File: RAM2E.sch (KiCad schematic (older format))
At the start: 54 parts, among them J1 AppleIIeAux, U1 EPM240T100, U2 W9864G6KH-6, U3 74AHC245, U4 74AHC245, U5 74AHC245, U6 74AHCT245, U7 74AHCT245, U8 TPS73701, U9 TPS73701

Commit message: Sent to JLCPCB
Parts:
- removed C? (x2): 2u2, stdpads:C_0603, symbol Device:C_Small
- added C29: 10u, stdpads:C_0805, symbol Device:C_Small
- added H5: (no value), stdpads:PasteHole_1.1mm_PTH, symbol Mechanical:MountingHole_Pad
- added J2: JTAG, Connector:Tag-Connect_TC2050-IDC-FP_2x05_P1.27mm_Vertical, symbol Connector_Generic:Conn_02x05_Odd_Even
- added R5, R7: DNP, stdpads:R_0805, symbol Device:R_Small
- added R6: 0, stdpads:R_0805, symbol Device:R_Small
- added RN1, RN2, RN3: 4x100, stdpads:Yageo_YC124, symbol Device:R_Pack04
- R1: value 1k2 -> 5k76
- R2, R3: value 1k2 -> 3k3
- R4: value 1k2 -> 6k8
- R8: renamed from R5; footprint (none) -> stdpads:R_0805
- U1: value EPM240T100 -> 5M240ZT100; footprint Package_QFP:LQFP-100_14x14mm_P0.5mm -> stdpads:TQFP-100_14x14mm_P0.5mm; symbol CPLD_Altera:EPM240T100 -> GW_PLD:5M240ZT100
- U2: footprint stdpads:Winbond_TSOPII-54 -> stdpads:TSOP-II-54_22.2x10.16mm_P0.8mm
- U3, U5, U6, U7: footprint (none) -> stdpads:TSSOP-20_4.4x6.5mm_P0.65mm
- U4: value 74AHC245 -> 74LVC245; footprint (none) -> stdpads:TSSOP-20_4.4x6.5mm_P0.65mm
- gave numbers to parts that had none: 2
- renumbered C31 to C30
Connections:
- net labels added: ACLK, DlyIn, DlyOut, RCLK, RD0r, RD1r, RD2r, RD3r, RD4r, RD5r, RD6r, RD7r, TCK, TDI, TDO, TMS
- net labels removed: CLK
- wire segments 218 -> 276
- no-connect marks 6 -> 11
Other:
- moved on the sheet: C1, C10, C11, C12, C13, C14, C15, C16, C17, C18, C19, C2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

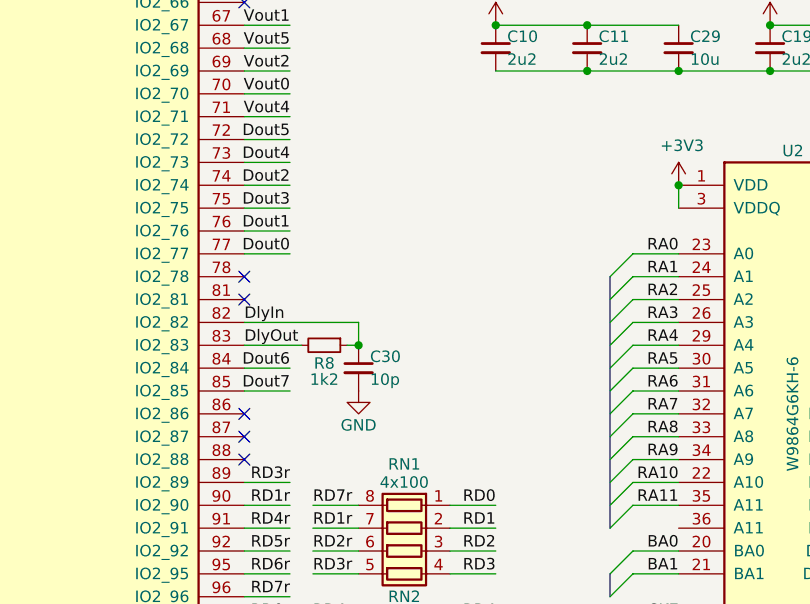
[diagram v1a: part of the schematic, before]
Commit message: Fixed board GW number silkscreen, added config jumpers
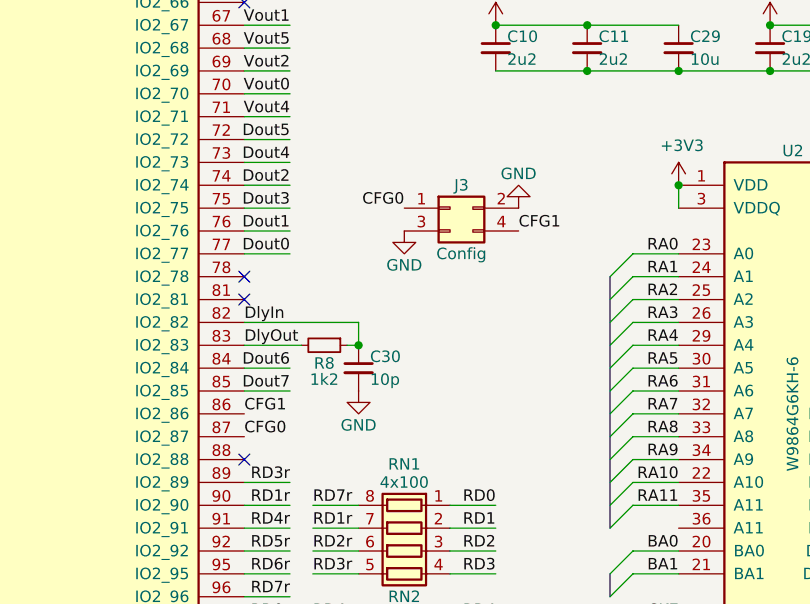
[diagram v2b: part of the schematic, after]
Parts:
- added J3: Config, Connector_PinHeader_2.54mm:PinHeader_2x02_P2.54mm_Vertical_SMD, symbol Connector_Generic:Conn_02x02_Odd_Even
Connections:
- net GND: now also J3.2 (Pin_2), J3.3 (Pin_3)
- net CFG1: now reaches U1.86 (IO2_86)
- net CFG1: now also J3.4 (Pin_4)
- net CFG0: now reaches U1.87 (IO2_87)
- net CFG0: now also J3.1 (Pin_1)
- no-connect marks 11 -> 9
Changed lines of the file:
@@
 RD3
 NoConn ~ 6600 5050
-NoConn ~ 6600 4950
-NoConn ~ 6600 4850
 $Comp
 L power:GND #PWR0108
@@
 	1    0    0    -1
 $EndComp
+Text Label 6600 4850 0    50   ~ 0
+CFG1
+Text Label 6600 4950 0    50   ~ 0
+CFG0
+$Comp
+L Connector_Generic:Conn_02x02_Odd_Even J3
+U 1 1 5EA8BDCC
+P 7500 3950
+F 0 "J3" H 7550 4050 50  0000 C CNN
+F 1 "Config" H 7550 3750 50  0000 C CNN
+F 2 "Connector_PinHeader_2.54mm:PinHeader_2x02_P2.54mm_Vertical_SMD" H 7500 3950 50  0001 C CNN
+F 3 "~" H 7500 3950 50  0001 C CNN
+	1    7500 3950
+	1    0    0    -1
+$EndComp
+Text Label 7300 3950 2    50   ~ 0
+CFG0
+Text Label 7800 4050 0    50   ~ 0
+CFG1
 Wire Bus Line
 	8200 4250 8200 5350
+$Comp
+L power:GND #PWR0146
+U 1 1 5EAAE8A3
+P 7300 4050
+F 0 "#PWR0146" H 7300 3800 50  0001 C CNN
+F 1 "GND" H 7300 3900 50  0000 C CNN
+F 2 "" H 7300 4050 50  0001 C CNN
+F 3 "" H 7300 4050 50  0001 C CNN
+	1    7300 4050
+	1    0    0    -1
+$EndComp
+$Comp
+L power:GND #PWR0147
+U 1 1 5EAAEC35
+P 7800 3950
+F 0 "#PWR0147" H 7800 3700 50  0001 C CNN
+F 1 "GND" H 7800 3800 50  0000 C CNN
+F 2 "" H 7800 3950 50  0001 C CNN
+F 3 "" H 7800 3950 50  0001 C CNN
+	1    7800 3950
+	-1   0    0    1
+$EndComp
 $EndSCHEMATC

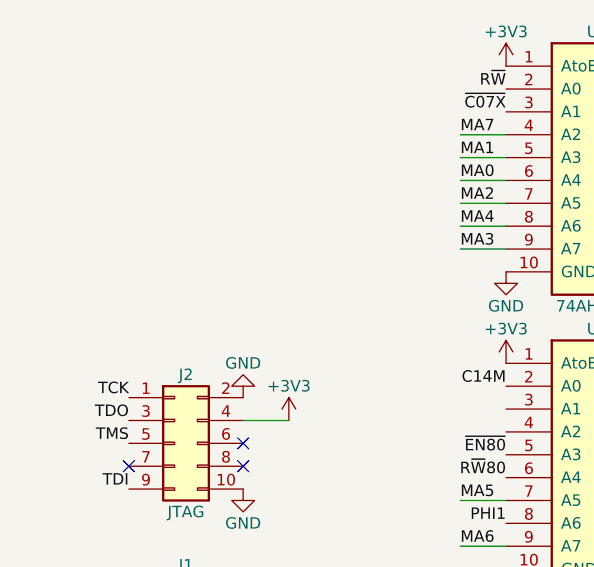
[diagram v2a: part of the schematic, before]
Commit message: Added jumper, new state machine docs
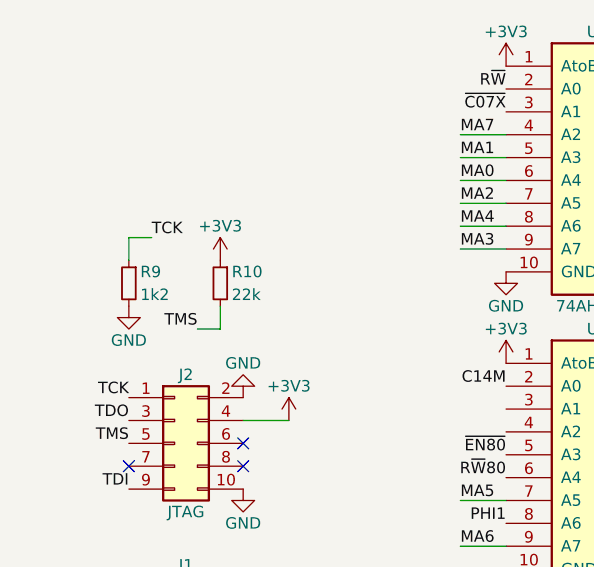
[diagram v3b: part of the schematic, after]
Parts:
- added R10: 22k, stdpads:R_0805, symbol Device:R_Small
- added R9: 1k2, stdpads:R_0805, symbol Device:R_Small
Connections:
- net +3V3: now also R10.1
- net GND: now also R9.2
- net TCK: now also R9.1
- net TMS: now also R10.2
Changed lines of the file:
@@
 encoding utf-8
 Sheet 1 2
-Title "RAM2E"
-Date "2019-10-13"
+Title "RAM2E II"
+Date "2020-05-06"
 Rev "0.9"
 Comp "Garrett's Workshop"
@@
 Text Label 7800 4050 0    50   ~ 0
 CFG1
-Wire Bus Line
-	8200 4250 8200 5350
 $Comp
 L power:GND #PWR0146
@@
 	-1   0    0    1
 $EndComp
+$Comp
+L Device:R_Small R9
+U 1 1 5EBE988D
+P 950 2000
+F 0 "R9" H 900 2050 50  0000 R CNN
+F 1 "1k2" H 900 1950 50  0000 R CNN
+F 2 "stdpads:R_0805" H 950 2000 50  0001 C CNN
+F 3 "~" H 950 2000 50  0001 C CNN
+	1    950  2000
+	-1   0    0    -1
+$EndComp
+$Comp
+L Device:R_Small R10
+U 1 1 5EBEA685
+P 1350 2000
+F 0 "R10" H 1300 2050 50  0000 R CNN
+F 1 "22k" H 1300 1950 50  0000 R CNN
+F 2 "stdpads:R_0805" H 1350 2000 50  0001 C CNN
+F 3 "~" H 1350 2000 50  0001 C CNN
+	1    1350 2000
+	-1   0    0    -1
+$EndComp
+$Comp
+L power:GND #PWR?
+U 1 1 5EBEEA76
+P 950 2100
+F 0 "#PWR?" H 950 1850 50  0001 C CNN
+F 1 "GND" H 950 1950 50  0000 C CNN
+F 2 "" H 950 2100 50  0001 C CNN
+F 3 "" H 950 2100 50  0001 C CNN
+	1    950  2100
+	1    0    0    -1
+$EndComp
+$Comp
+L power:+3V3 #PWR?
+U 1 1 5EBEF11E
+P 1350 1900
+F 0 "#PWR?" H 1350 1750 50  0001 C CNN
+F 1 "+3V3" H 1350 2050 50  0000 C CNN
+F 2 "" H 1350 1900 50  0001 C CNN
+F 3 "" H 1350 1900 50  0001 C CNN
+	1    1350 1900
+	1    0    0    -1
+$EndComp
+Text Label 1250 2200 2    50   ~ 0
+TMS
+Wire Wire Line
+	1250 2200 1350 2200
+Wire Wire Line
+	1350 2200 1350 2100
+Wire Wire Line
+	950  1900 950  1800
+Wire Wire Line
+	950  1800 1050 1800
+Wire Bus Line
+	8200 4250 8200 5350
+Text Label 1050 1800 0    50   ~ 0
+TCK
 $EndSCHEMATC
